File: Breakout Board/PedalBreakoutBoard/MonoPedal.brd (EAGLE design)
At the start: 65.7 x 61 mm, 52 parts, among them IC1 LD1117V, IC2 MCP6004P, U1 OPA1652AID

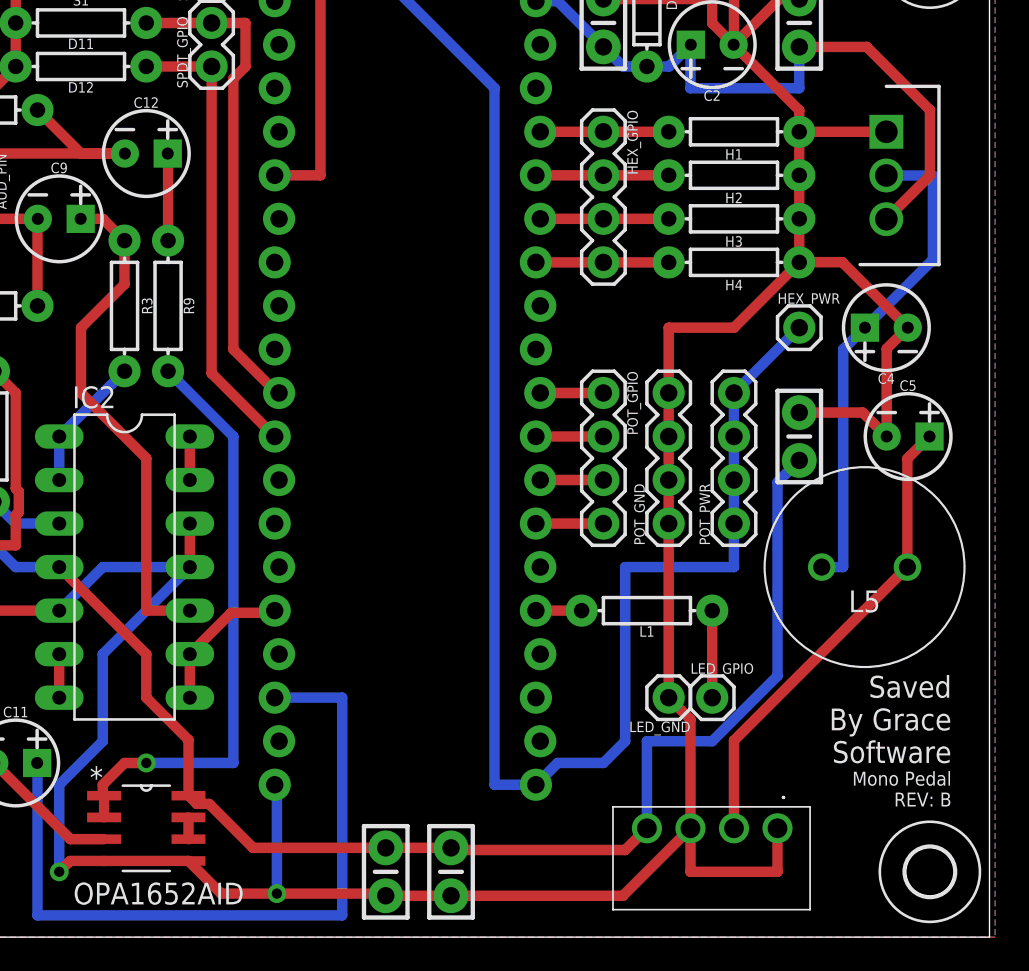
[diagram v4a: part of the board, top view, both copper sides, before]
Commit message: DP-34 - Fixing silk screen errors
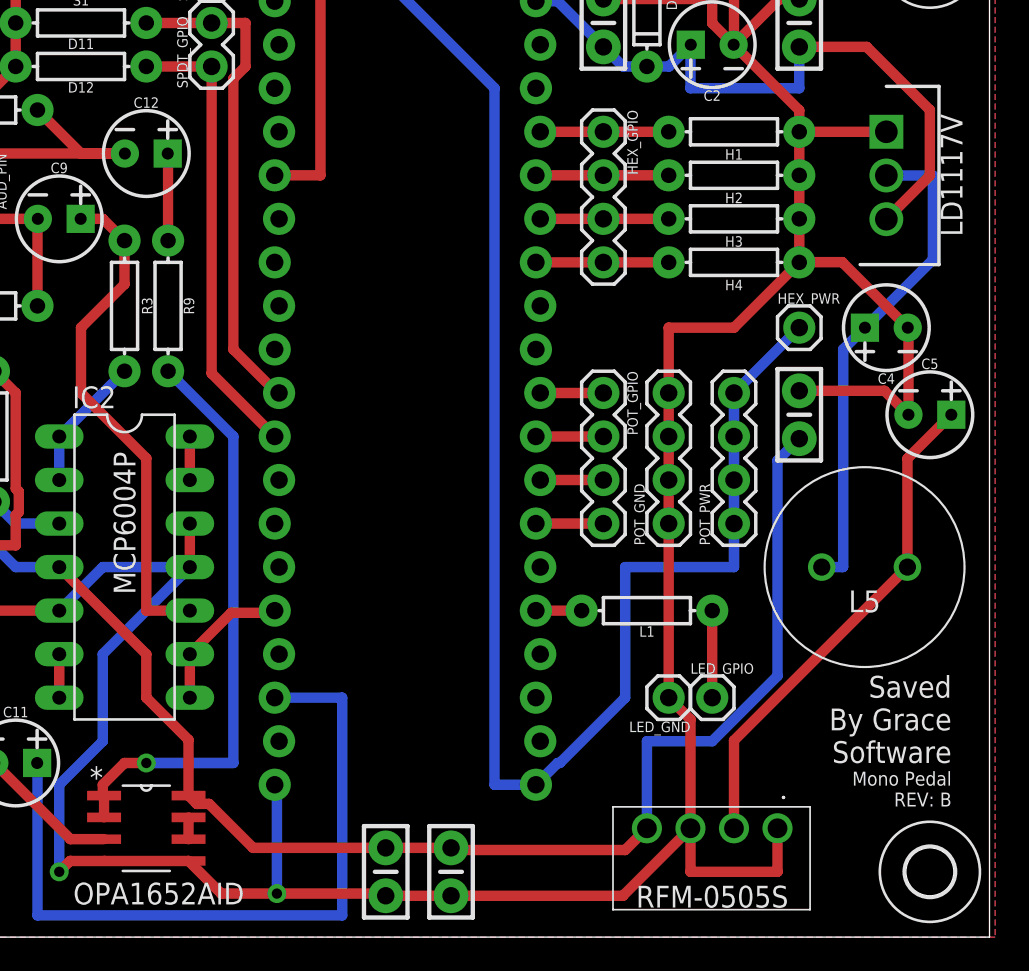
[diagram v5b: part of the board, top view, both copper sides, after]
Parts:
- moved C5 1.80 mm to (62.2, 30.5)
- moved C6 1.27 mm to (54.6, 30.5)
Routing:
- net N$7: track 27.6 -> 29.4 mm
- net +3V3_A: track 111.5 -> 110.0 mm
- net +5V_ISOL: track 89.0 -> 90.3 mm
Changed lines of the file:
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@@
 <attribute name="PROD_ID" value="CAP-08440" x="36.83" y="107.95" size="1.778" layer="27" rot="R180" display="off"/>
 </element>
-<element name="C5" library="SparkFun-Capacitors" library_urn="urn:adsk.eagle:library:510" package="CPOL-RADIAL-2.5MM-5MM" package3d_urn="urn:adsk.eagle:package:37423/1" value="10uF" x="60.96" y="29.21" smashed="yes">
-<attribute name="NAME" x="60.96" y="31.877" size="0.6096" layer="25" font="vector" ratio="20" align="bottom-center"/>
-<attribute name="PROD_ID" value="CAP-08440" x="90.17" y="-43.18" size="1.778" layer="27" display="off"/>
-</element>
-<element name="C6" library="Custom-Parts" package="CAP-PTH-SMALL-KIT" value="22UF" x="54.61" y="29.21" smashed="yes" rot="R90"/>
+<element name="C5" library="SparkFun-Capacitors" library_urn="urn:adsk.eagle:library:510" package="CPOL-RADIAL-2.5MM-5MM" package3d_urn="urn:adsk.eagle:package:37423/1" value="10uF" x="62.23" y="30.48" smashed="yes">
+<attribute name="NAME" x="62.23" y="33.147" size="0.6096" layer="25" font="vector" ratio="20" align="bottom-center"/>
+<attribute name="PROD_ID" value="CAP-08440" x="91.44" y="-41.91" size="1.778" layer="27" display="off"/>
+</element>
+<element name="C6" library="Custom-Parts" package="CAP-PTH-SMALL-KIT" value="22UF" x="54.61" y="30.48" smashed="yes" rot="R90"/>
 <element name="C7" library="SparkFun-Capacitors" library_urn="urn:adsk.eagle:library:510" package="CAP-PTH-SMALL-KIT" package3d_urn="urn:adsk.eagle:package:37428/1" value="0.1uF" x="30.48" y="3.81" smashed="yes" rot="R270">
 <attribute name="PROD_ID" value="CAP-08370" x="-66.04" y="-57.15" size="1.778" layer="27" rot="R270" display="name"/>
@@
 <attribute name="MOUSER_PART_NUMBER" value="511-LD1117V" x="-19.05" y="25.4" size="1.778" layer="27" rot="R270" display="off"/>
 <attribute name="MOUSER_PRICE-STOCK" value="https://www.mouser.co.uk/ProductDetail/STMicroelectronics/LD1117V?qs=tZUCD5p2VWqhC74a4KMNzA%3D%3D" x="-19.05" y="25.4" size="1.778" layer="27" rot="R270" display="off"/>
-<attribute name="VALUE" x="63.5" y="44.45" size="1.27" layer="27" rot="R270" align="center"/>
+<attribute name="VALUE" x="63.5" y="44.45" size="1.27" layer="25" rot="R270" align="center"/>
 </element>
 <element name="IC2" library="Custom-Parts" package="DIL14" package3d_urn="urn:adsk.eagle:package:16407/2" value="MCP6004P" x="15.24" y="21.59" smashed="yes" rot="R270">
 <attribute name="NAME" x="12.192" y="30.861" size="1.27" layer="25" ratio="10"/>
 <attribute name="POPULARITY" value="0" x="-48.26" y="-1.27" size="1.778" layer="27" rot="R270" display="off"/>
-<attribute name="VALUE" x="14.605" y="28.321" size="1.27" layer="27" ratio="10" rot="R270"/>
+<attribute name="VALUE" x="14.605" y="28.321" size="1.27" layer="25" ratio="10" rot="R270"/>
 </element>
 <element name="L1" library="SparkFun-Resistors" library_urn="urn:adsk.eagle:library:532" package="AXIAL-0.3" package3d_urn="urn:adsk.eagle:package:39658/1" value="330" x="45.72" y="19.05" smashed="yes">
@@
 <attribute name="MOUSER_PART_NUMBER" value="919-RFM-0505S" x="7.62" y="67.31" size="1.778" layer="27" rot="R180" display="off"/>
 <attribute name="MOUSER_PRICE-STOCK" value="https://www.mouser.co.uk/ProductDetail/RECOM-Power/RFM-0505S?qs=lYGu3FyN48dRVYKTH5ipqg%3D%3D" x="7.62" y="67.31" size="1.778" layer="27" rot="R180" display="off"/>
-<attribute name="VALUE" x="49.53" y="2.36" size="1.27" layer="27" rot="R180" align="center"/>
+<attribute name="VALUE" x="49.53" y="2.36" size="1.27" layer="25" rot="R180" align="center"/>
 </element>
 <element name="PWR" library="SparkFun-Connectors" library_urn="urn:adsk.eagle:library:513" package="1X02" package3d_urn="urn:adsk.eagle:package:38039/1" value="" x="50.8" y="58.42" smashed="yes" rot="R180">
@@
 <wire x1="46.99" y1="13.97" x2="48.26" y2="12.7" width="0.6096" layer="1"/>
 <wire x1="48.26" y1="12.7" x2="48.26" y2="6.35" width="0.6096" layer="1"/>
-<wire x1="60.94" y1="35.56" x2="59.71" y2="34.33" width="0.6096" layer="1"/>
-<wire x1="59.71" y1="34.33" x2="59.71" y2="29.21" width="0.6096" layer="1"/>
+<wire x1="60.94" y1="35.56" x2="60.98" y2="35.52" width="0.6096" layer="1"/>
+<wire x1="60.98" y1="35.52" x2="60.98" y2="30.48" width="0.6096" layer="1"/>
 <wire x1="11.43" y1="19.05" x2="13.97" y2="21.59" width="0.6096" layer="16"/>
 <wire x1="13.97" y1="21.59" x2="19.05" y2="21.59" width="0.6096" layer="16"/>
@@
 <wire x1="54.6227" y1="39.3827" x2="54.61" y2="39.37" width="0.6096" layer="1"/>
 <wire x1="57.1173" y1="39.3827" x2="54.6227" y2="39.3827" width="0.6096" layer="1"/>
-<wire x1="54.61" y1="30.607" x2="58.313" y2="30.607" width="0.6096" layer="1"/>
-<wire x1="58.313" y1="30.607" x2="59.71" y2="29.21" width="0.6096" layer="1"/>
+<wire x1="54.61" y1="31.877" x2="59.583" y2="31.877" width="0.6096" layer="1"/>
+<wire x1="59.583" y1="31.877" x2="60.98" y2="30.48" width="0.6096" layer="1"/>
 <wire x1="50.78" y1="52.07" x2="53.447" y2="54.737" width="0.6096" layer="1"/>
 <wire x1="53.447" y1="54.737" x2="54.61" y2="54.737" width="0.6096" layer="1"/>
@@
 <wire x1="16.51" y1="58.42" x2="11.43" y2="58.42" width="0.6096" layer="16"/>
 <wire x1="39.243" y1="8.89" x2="40.513" y2="10.16" width="0.6096" layer="16"/>
-<wire x1="40.513" y1="10.16" x2="43.18" y2="10.16" width="0.6096" layer="16"/>
-<wire x1="43.18" y1="10.16" x2="44.45" y2="11.43" width="0.6096" layer="16"/>
-<wire x1="44.45" y1="11.43" x2="44.45" y2="21.59" width="0.6096" layer="16"/>
+<wire x1="40.513" y1="10.16" x2="40.64" y2="10.16" width="0.6096" layer="16"/>
+<wire x1="40.64" y1="10.16" x2="44.45" y2="13.97" width="0.6096" layer="16"/>
+<wire x1="44.45" y1="13.97" x2="44.45" y2="21.59" width="0.6096" layer="16"/>
 <wire x1="44.45" y1="21.59" x2="50.8" y2="21.59" width="0.6096" layer="16"/>
 <wire x1="50.8" y1="21.59" x2="50.8" y2="24.13" width="0.6096" layer="16"/>
@@
 <contactref element="PS1" pad="2"/>
 <wire x1="60.92" y1="21.59" x2="60.92" y2="27.92" width="0.6096" layer="1"/>
-<wire x1="60.92" y1="27.92" x2="62.21" y2="29.21" width="0.6096" layer="1"/>
+<wire x1="60.92" y1="27.92" x2="63.48" y2="30.48" width="0.6096" layer="1"/>
 <wire x1="50.8" y1="6.35" x2="50.8" y2="11.47" width="0.6096" layer="1"/>
 <wire x1="50.8" y1="11.47" x2="60.92" y2="21.59" width="0.6096" layer="1"/>
@@
 <wire x1="45.72" y1="6.35" x2="45.72" y2="11.43" width="0.6096" layer="16"/>
 <wire x1="45.72" y1="11.43" x2="49.53" y2="11.43" width="0.6096" layer="16"/>
-<wire x1="53.34" y1="26.543" x2="54.61" y2="27.813" width="0.6096" layer="16"/>
-<wire x1="53.34" y1="15.24" x2="53.34" y2="26.543" width="0.6096" layer="16"/>
+<wire x1="53.34" y1="27.813" x2="54.61" y2="29.083" width="0.6096" layer="16"/>
+<wire x1="53.34" y1="15.24" x2="53.34" y2="27.813" width="0.6096" layer="16"/>
 <wire x1="5.08" y1="25.4" x2="8.89" y2="21.59" width="0.6096" layer="16"/>
 <wire x1="8.89" y1="21.59" x2="11.43" y2="21.59" width="0.6096" layer="16"/>

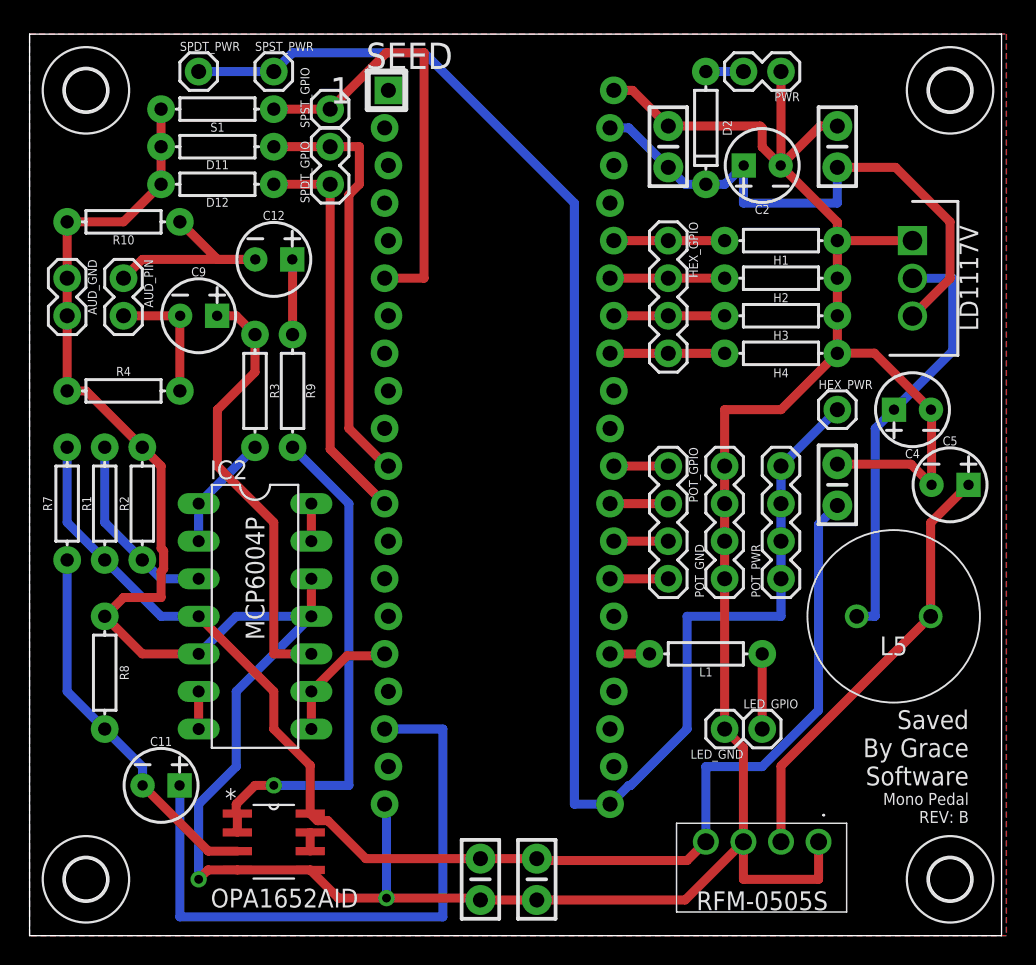
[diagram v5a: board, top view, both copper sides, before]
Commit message: DP-33 - Update mono pedal to ceramic 10uF capacitors
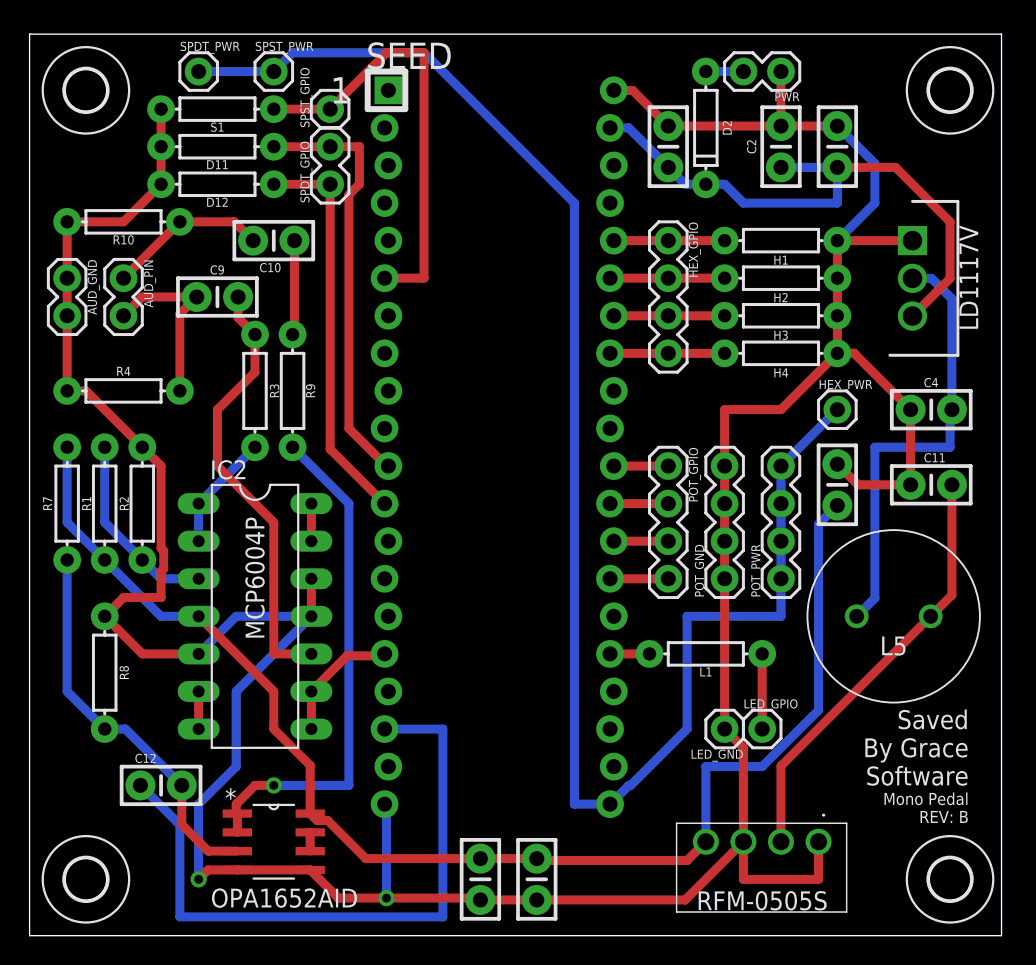
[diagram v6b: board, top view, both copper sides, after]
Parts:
- removed C5: 10uF, SparkFun-Capacitors:CPOL-RADIAL-2.5MM-5MM
- added C10: 10UF, Custom-Parts:CAP-PTH-SMALL-KIT
- C11, C12, C2, C4, C9: value 10uF -> 10UF; device SparkFun-Capacitors:CPOL-RADIAL-2.5MM-5MM -> Custom-Parts:CAP-PTH-SMALL-KIT
- moved C11 55.9 mm to (61.0, 30.5)
- moved C12 36.4 mm to (8.89, 10.2)
- moved C9 1.80 mm to (12.7, 43.2)
- moved C2 1.80 mm to (50.8, 53.3), turned to 270 degrees
- moved C4 1.27 mm to (61.0, 35.6), turned to 0 degrees
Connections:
- net +9V_IN: now also C2.2; no longer C2.1
- net GND: now also C11.1, C2.1, C4.1; no longer C2.2, C4.2, C5.2
- net IN_L_JACK: now also C9.1; no longer C9.2
- net N$12: now also C12.2; no longer C11.2
- net N$14: now also C10.1; no longer C12.1
- net N$7: now also C11.2; no longer C5.1
- net N$8: now also C4.2; no longer C4.1
- net N$9: now also C9.2; no longer C9.1
- net OUT_L: now also C12.1; no longer C11.1
- net OUT_L_JACK: now also C10.2; no longer C12.2
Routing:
- net GND: track 245.1 -> 239.9 mm
- net OUT_L_JACK: track 15.6 -> 10.9 mm
- net IN_L_JACK: track 8.92 -> 12.3 mm
- net N$8: track 29.0 -> 30.3 mm
- net N$14: track 5.09 -> 6.40 mm
- net +9V_IN: track 39.0 -> 40.3 mm
- net OUT_L: track 43.3 -> 44.4 mm
- net N$12: track 25.6 -> 26.4 mm
- removed copper zone on layer 1, net GND
- removed copper zone on layer 16, net GND

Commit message: DP-33 - Update mono pedal board with proper silk screen
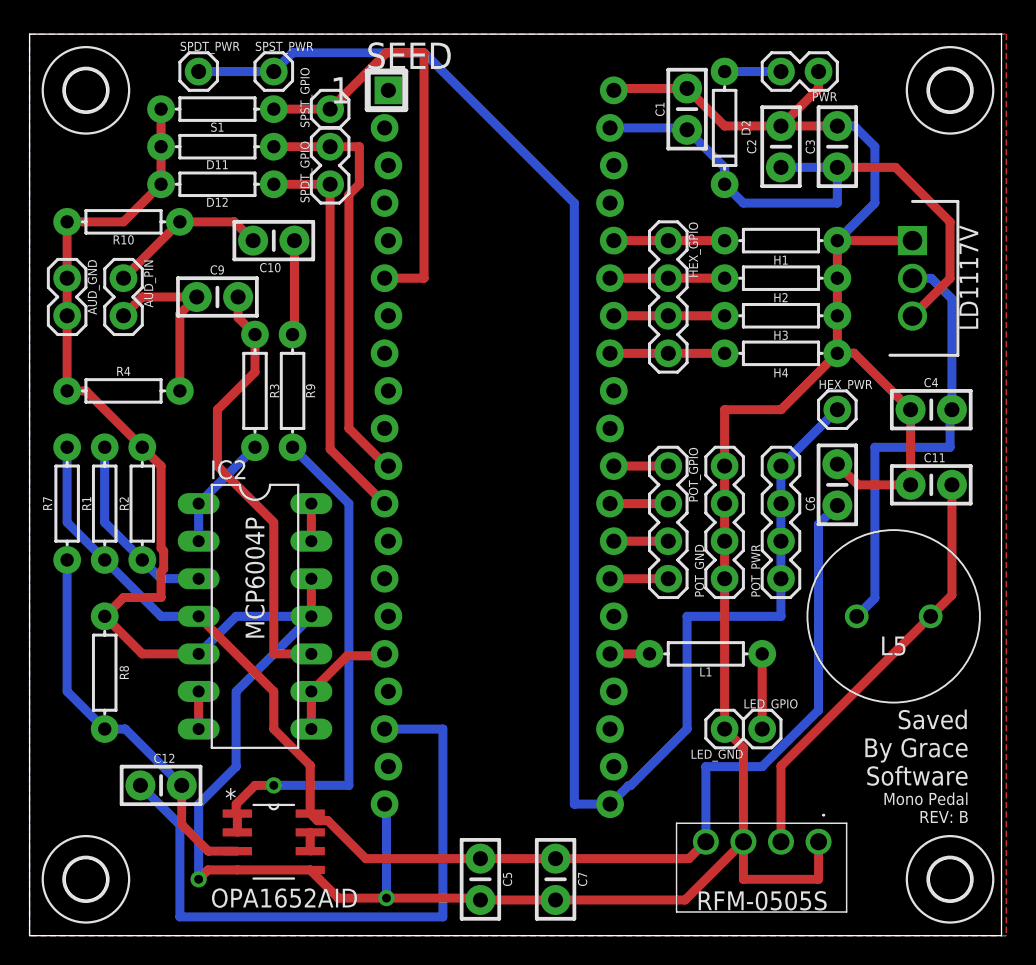
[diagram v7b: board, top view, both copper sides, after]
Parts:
- removed C8: 0.1uF, SparkFun-Capacitors:CAP-PTH-SMALL-KIT
- added C5: 0.1UF, Custom-Parts:CAP-PTH-SMALL-KIT
- C1, C3, C7: value 0.1uF -> 0.1UF; device SparkFun-Capacitors:CAP-PTH-SMALL-KIT -> Custom-Parts:CAP-PTH-SMALL-KIT
- moved C7 5.08 mm to (35.6, 3.81)
- moved C1 2.84 mm to (44.5, 55.9)
- moved PWR 2.54 mm to (53.3, 58.4)
- moved D2 1.27 mm to (47.0, 54.6)
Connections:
- net +5V_ISOL: now also C5.1; no longer C8.1
- net GND: now also C5.2; no longer C8.2
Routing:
- net GND: track 239.9 -> 241.7 mm
- net N$2: track 2.54 -> 3.81 mm
- net +9V_IN: track 40.3 -> 40.9 mm
- added copper zone on layer 1, net GND
- added copper zone on layer 16, net GND
